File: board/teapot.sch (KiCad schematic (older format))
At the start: 42 parts, among them P1 BATT, P2 SMA, Q1 TEPT4400, U1 TLV61225, U2 microusb-b, U3 RFM69W, U4 STM32L052K8, U5 HTU21D, U6 MS5637, U7 SWD, U8 TPS79333DBVR, Y1 32.768k

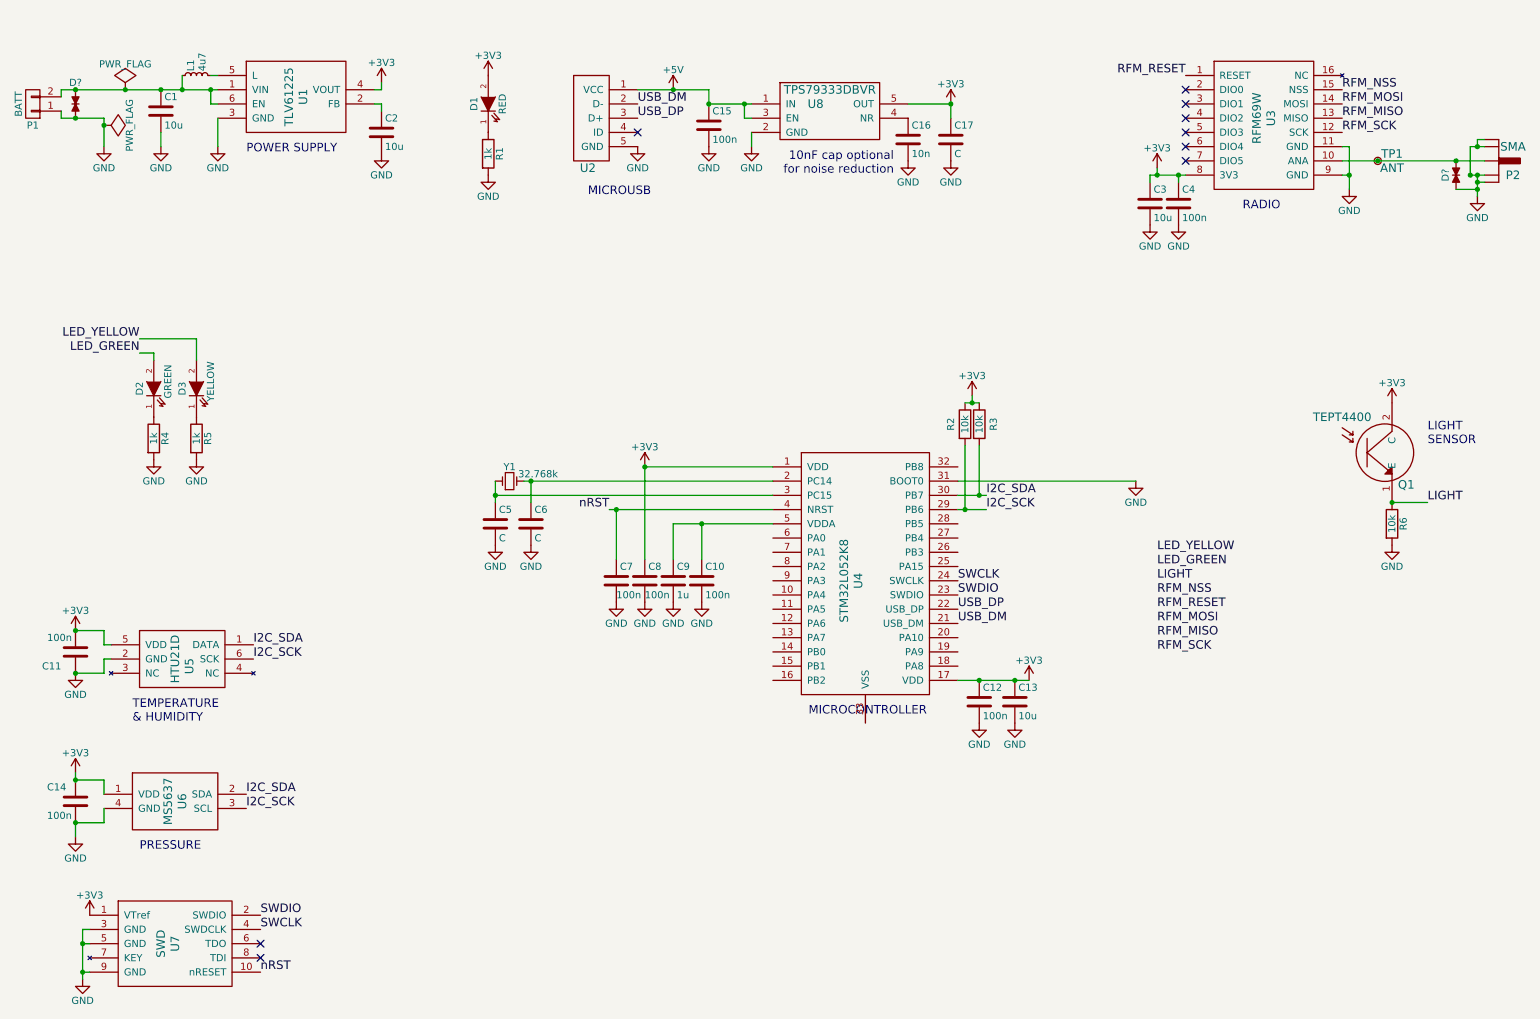
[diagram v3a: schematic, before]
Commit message: Finished speccings parts and footprints.
Resolves #3
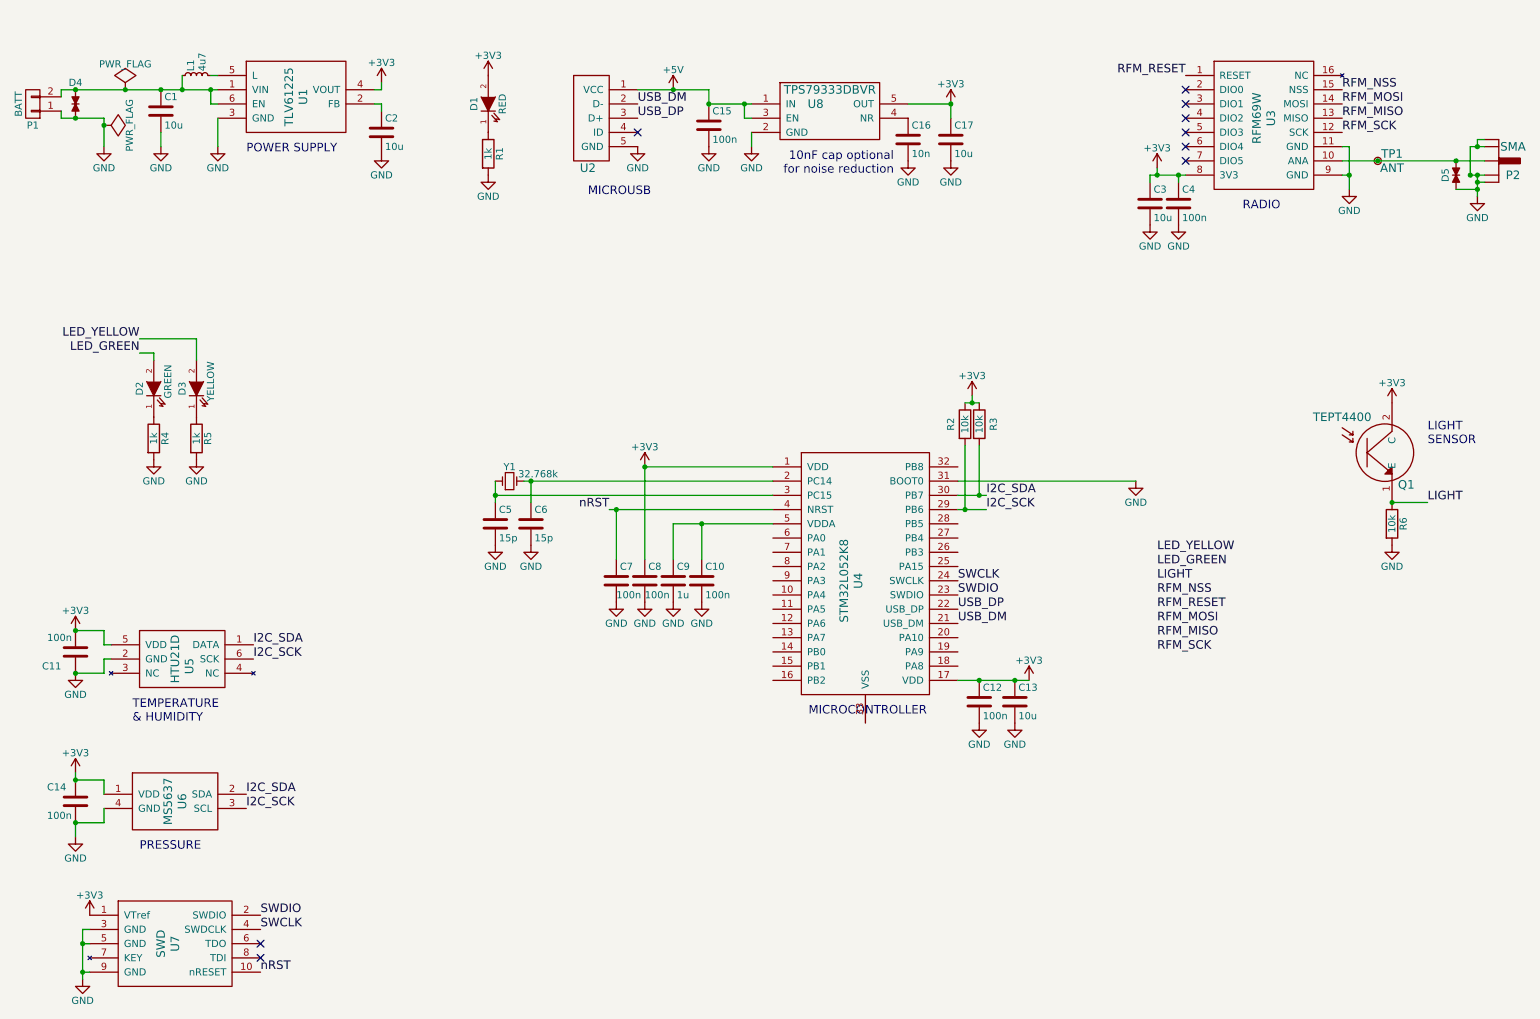
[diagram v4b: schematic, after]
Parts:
- C1, C2: footprint (none) -> Capacitors_SMD:C_0603
- C10, C11, C12, C14, C15, C4, C7, C8: footprint (none) -> Capacitors_SMD:C_0805; Farnell (none) -> 2407344
- C13, C3: footprint (none) -> Capacitors_SMD:C_0603; Farnell (none) -> 1735528
- C17: value C -> 10u; footprint (none) -> Capacitors_SMD:C_0603; Farnell (none) -> 1735528
- C5, C6: value C -> 15p; footprint (none) -> Capacitors_SMD:C_0805; Farnell (none) -> 1759193
- C9: footprint (none) -> Capacitors_SMD:C_0805; Farnell (none) -> 2496995
- D1: footprint (none) -> LEDs:LED-0805; Farnell (none) -> 2099241
- D2: footprint (none) -> LEDs:LED-0805; Farnell (none) -> 2290331
- D3: footprint (none) -> LEDs:LED-0805; Farnell (none) -> 2099242
- L1: footprint (none) -> footprints:Inductor_1212
- R1, R4, R5: footprint (none) -> Resistors_SMD:R_0805; Farnell (none) -> 2331796
- R2, R3, R6: footprint (none) -> Resistors_SMD:R_0805; Farnell (none) -> 2502786
- U2: Farnell (none) -> 2443111
- Y1: footprint (none) -> footprints:XTAL_1206
- gave numbers to parts that had none: 2
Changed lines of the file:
@@
 F 0 "C11" H 1050 5150 50  0000 L CNN
 F 1 "100n" H 975 4950 50  0000 L CNN
-F 2 "" H 988 4900 50  0000 C CNN
+F 2 "Capacitors_SMD:C_0805" H 988 4900 50  0001 C CNN
 F 3 "" H 950 5050 50  0000 C CNN
+F 4 "2407344" H 950 5050 60  0001 C CNN "Farnell"
 	1    950  5050
 	-1   0    0    1
@@
 F 0 "C2" H 3125 1500 50  0000 L CNN
 F 1 "10u" H 3125 1300 50  0000 L CNN
-F 2 "" H 3138 1250 50  0000 C CNN
-F 3 "" H 3100 1400 50  0000 C CNN
+F 2 "Capacitors_SMD:C_0603" H 3138 1250 50  0001 C CNN
+F 3 "http://www.farnell.com/datasheets/1747457.pdf" H 3100 1400 50  0001 C CNN
 F 4 "1735528" H 3100 1400 60  0001 C CNN "Farnell"
 	1    3100 1400
@@
 F 0 "C1" H 1575 1350 50  0000 L CNN
 F 1 "10u" H 1575 1150 50  0000 L CNN
-F 2 "" H 1588 1100 50  0000 C CNN
-F 3 "" H 1550 1250 50  0000 C CNN
+F 2 "Capacitors_SMD:C_0603" H 1588 1100 50  0001 C CNN
+F 3 "http://www.farnell.com/datasheets/1747457.pdf" H 1550 1250 50  0001 C CNN
 F 4 "1735528" H 1550 1250 60  0001 C CNN "Farnell"
 	1    1550 1250
@@
 F 0 "L1" H 1830 1040 50  0000 L CNN
 F 1 "4u7" H 1830 960 50  0000 L CNN
-F 2 "" H 1800 1000 50  0000 C CNN
-F 3 "" H 1800 1000 50  0000 C CNN
+F 2 "footprints:Inductor_1212" H 1800 1000 50  0001 C CNN
+F 3 "http://www.farnell.com/datasheets/1888724.pdf" H 1800 1000 50  0001 C CNN
 F 4 "2470318" H 1800 1000 60  0001 C CNN "Farnell"
 	1    1800 1000
@@
 F 0 "R3" V 7400 3450 50  0000 C CNN
 F 1 "10k" V 7300 3450 50  0000 C CNN
-F 2 "" V 7230 3450 50  0000 C CNN
+F 2 "Resistors_SMD:R_0805" V 7230 3450 50  0001 C CNN
 F 3 "" H 7300 3450 50  0000 C CNN
+F 4 "2502786" H 7300 3450 60  0001 C CNN "Farnell"
 	1    7300 3450
 	1    0    0    -1
@@
 F 0 "R2" V 7100 3450 50  0000 C CNN
 F 1 "10k" V 7200 3450 50  0000 C CNN
-F 2 "" V 7130 3450 50  0000 C CNN
+F 2 "Resistors_SMD:R_0805" V 7130 3450 50  0001 C CNN
 F 3 "" H 7200 3450 50  0000 C CNN
+F 4 "2502786" H 7200 3450 60  0001 C CNN "Farnell"
 	1    7200 3450
 	1    0    0    -1
@@
 F 0 "C14" H 750 6200 50  0000 L CNN
 F 1 "100n" H 750 6000 50  0000 L CNN
-F 2 "" H 988 5950 50  0000 C CNN
+F 2 "Capacitors_SMD:C_0805" H 988 5950 50  0001 C CNN
 F 3 "" H 950 6100 50  0000 C CNN
+F 4 "2407344" H 950 6100 60  0001 C CNN "Farnell"
 	1    950  6100
 	1    0    0    -1
@@
 F 0 "R6" V 10280 4150 50  0000 C CNN
 F 1 "10k" V 10200 4150 50  0000 C CNN
-F 2 "" V 10130 4150 50  0000 C CNN
+F 2 "Resistors_SMD:R_0805" V 10130 4150 50  0001 C CNN
 F 3 "" H 10200 4150 50  0000 C CNN
+F 4 "2502786" H 10200 4150 60  0001 C CNN "Farnell"
 	1    10200 4150
 	1    0    0    -1
@@
 F 1 "RFM69W" V 9250 1300 60  0000 C CNN
 F 2 "footprints:RFM69" H 9350 1750 60  0001 C CNN
-F 3 "https://hasnet.supplies/static/RFM69W-V1.3.pdf" H 9350 1750 60  0001 C CNN
+F 3 "http://www.hoperf.com/upload/rf/RFM69W-V1.3.pdf" H 9350 1750 60  0001 C CNN
 	1    9300 1300
 	1    0    0    -1
@@
 F 0 "C4" H 8725 2000 50  0000 L CNN
 F 1 "100n" H 8725 1800 50  0000 L CNN
-F 2 "" H 8738 1750 50  0000 C CNN
+F 2 "Capacitors_SMD:C_0805" H 8738 1750 50  0001 C CNN
 F 3 "" H 8700 1900 50  0000 C CNN
+F 4 "2407344" H 8700 1900 60  0001 C CNN "Farnell"
 	1    8700 1900
 	1    0    0    -1
@@
 F 0 "C3" H 8525 2000 50  0000 L CNN
 F 1 "10u" H 8525 1800 50  0000 L CNN
-F 2 "" H 8538 1750 50  0000 C CNN
-F 3 "" H 8500 1900 50  0000 C CNN
+F 2 "Capacitors_SMD:C_0603" H 8538 1750 50  0001 C CNN
+F 3 "http://www.farnell.com/datasheets/1747457.pdf" H 8500 1900 50  0001 C CNN
+F 4 "1735528" H 8500 1900 60  0001 C CNN "Farnell"
 	1    8500 1900
 	1    0    0    -1
@@
 F 0 "D1" H 3850 1300 50  0000 C CNN
 F 1 "RED" H 3850 1100 50  0000 C CNN
-F 2 "" H 3850 1200 50  0000 C CNN
+F 2 "LEDs:LED-0805" H 3850 1200 50  0001 C CNN
 F 3 "" H 3850 1200 50  0000 C CNN
+F 4 "2099241" H 3850 1200 60  0001 C CNN "Farnell"
 	1    3850 1200
 	0    -1   -1   0
@@
 F 0 "R1" V 3930 1550 50  0000 C CNN
 F 1 "1k" V 3850 1550 50  0000 C CNN
-F 2 "" V 3780 1550 50  0000 C CNN
+F 2 "Resistors_SMD:R_0805" V 3780 1550 50  0001 C CNN
 F 3 "" H 3850 1550 50  0000 C CNN
+F 4 "2331796" H 3850 1550 60  0001 C CNN "Farnell"
 	1    3850 1550
 	1    0    0    -1
@@
 F 0 "D2" H 1500 3300 50  0000 C CNN
 F 1 "GREEN" H 1550 3100 50  0000 C CNN
-F 2 "" H 1500 3200 50  0000 C CNN
+F 2 "LEDs:LED-0805" H 1500 3200 50  0001 C CNN
 F 3 "" H 1500 3200 50  0000 C CNN
+F 4 "2290331" H 1500 3200 60  0001 C CNN "Farnell"
 	1    1500 3200
 	0    -1   -1   0
@@
 F 0 "D3" H 1800 3300 50  0000 C CNN
 F 1 "YELLOW" H 1850 3100 50  0000 C CNN
-F 2 "" H 1800 3200 50  0000 C CNN
+F 2 "LEDs:LED-0805" H 1800 3200 50  0001 C CNN
 F 3 "" H 1800 3200 50  0000 C CNN
+F 4 "2099242" H 1800 3200 60  0001 C CNN "Farnell"
 	1    1800 3200
 	0    -1   -1   0
@@
 F 0 "R4" V 1580 3550 50  0000 C CNN
 F 1 "1k" V 1500 3550 50  0000 C CNN
-F 2 "" V 1430 3550 50  0000 C CNN
+F 2 "Resistors_SMD:R_0805" V 1430 3550 50  0001 C CNN
 F 3 "" H 1500 3550 50  0000 C CNN
+F 4 "2331796" H 1500 3550 60  0001 C CNN "Farnell"
 	1    1500 3550
 	1    0    0    -1
@@
 F 0 "R5" V 1880 3550 50  0000 C CNN
 F 1 "1k" V 1800 3550 50  0000 C CNN
-F 2 "" V 1730 3550 50  0000 C CNN
+F 2 "Resistors_SMD:R_0805" V 1730 3550 50  0001 C CNN
 F 3 "" H 1800 3550 50  0000 C CNN
+F 4 "2331796" H 1800 3550 60  0001 C CNN "Farnell"
 	1    1800 3550
 	1    0    0    -1
@@
 F 0 "C7" H 4775 4650 50  0000 L CNN
 F 1 "100n" H 4750 4450 50  0000 L CNN
-F 2 "" H 4788 4400 50  0000 C CNN
+F 2 "Capacitors_SMD:C_0805" H 4788 4400 50  0001 C CNN
 F 3 "" H 4750 4550 50  0000 C CNN
+F 4 "2407344" H 4750 4550 60  0001 C CNN "Farnell"
 	1    4750 4550
 	1    0    0    -1
@@
 F 0 "C8" H 4975 4650 50  0000 L CNN
 F 1 "100n" H 4950 4450 50  0000 L CNN
-F 2 "" H 4988 4400 50  0000 C CNN
+F 2 "Capacitors_SMD:C_0805" H 4988 4400 50  0001 C CNN
 F 3 "" H 4950 4550 50  0000 C CNN
+F 4 "2407344" H 4950 4550 60  0001 C CNN "Farnell"
 	1    4950 4550
 	1    0    0    -1
@@
 F 0 "C12" H 7325 5500 50  0000 L CNN
 F 1 "100n" H 7325 5300 50  0000 L CNN
-F 2 "" H 7338 5250 50  0000 C CNN
+F 2 "Capacitors_SMD:C_0805" H 7338 5250 50  0001 C CNN
 F 3 "" H 7300 5400 50  0000 C CNN
+F 4 "2407344" H 7300 5400 60  0001 C CNN "Farnell"
 	1    7300 5400
 	1    0    0    -1
@@
 F 0 "C13" H 7575 5500 50  0000 L CNN
 F 1 "10u" H 7575 5300 50  0000 L CNN
-F 2 "" H 7588 5250 50  0000 C CNN
-F 3 "" H 7550 5400 50  0000 C CNN
+F 2 "Capacitors_SMD:C_0603" H 7588 5250 50  0001 C CNN
+F 3 "http://www.farnell.com/datasheets/1747457.pdf" H 7550 5400 50  0001 C CNN
+F 4 "1735528" H 7550 5400 60  0001 C CNN "Farnell"
 	1    7550 5400
 	1    0    0    -1
@@
 F 0 "C9" H 5175 4650 50  0000 L CNN
 F 1 "1u" H 5175 4450 50  0000 L CNN
-F 2 "" H 5188 4400 50  0000 C CNN
+F 2 "Capacitors_SMD:C_0805" H 5188 4400 50  0001 C CNN
 F 3 "" H 5150 4550 50  0000 C CNN
+F 4 "2496995" H 5150 4550 60  0001 C CNN "Farnell"
 	1    5150 4550
 	1    0    0    -1
@@
 F 0 "C10" H 5375 4650 50  0000 L CNN
 F 1 "100n" H 5375 4450 50  0000 L CNN
-F 2 "" H 5388 4400 50  0000 C CNN
+F 2 "Capacitors_SMD:C_0805" H 5388 4400 50  0001 C CNN
 F 3 "" H 5350 4550 50  0000 C CNN
+F 4 "2407344" H 5350 4550 60  0001 C CNN "Farnell"
 	1    5350 4550
 	1    0    0    -1
@@
 F 0 "Y1" H 4000 3950 50  0000 C CNN
 F 1 "32.768k" H 4200 3900 50  0000 C CNN
-F 2 "" H 4000 3850 50  0000 C CNN
+F 2 "footprints:XTAL_1206" H 4000 3850 50  0001 C CNN
 F 3 "http://www.farnell.com/datasheets/1883680.pdf" H 4000 3850 50  0001 C CNN
 F 4 "2101347" H 4000 3850 60  0001 C CNN "Farnell"
@@
 P 3900 4150
 F 0 "C5" H 3925 4250 50  0000 L CNN
-F 1 "C" H 3925 4050 50  0000 L CNN
-F 2 "" H 3938 4000 50  0000 C CNN
+F 1 "15p" H 3925 4050 50  0000 L CNN
+F 2 "Capacitors_SMD:C_0805" H 3938 4000 50  0001 C CNN
 F 3 "" H 3900 4150 50  0000 C CNN
+F 4 "1759193" H 3900 4150 60  0001 C CNN "Farnell"
 	1    3900 4150
 	1    0    0    -1
@@
 P 4150 4150
 F 0 "C6" H 4175 4250 50  0000 L CNN
-F 1 "C" H 4175 4050 50  0000 L CNN
-F 2 "" H 4188 4000 50  0000 C CNN
+F 1 "15p" H 4175 4050 50  0000 L CNN
+F 2 "Capacitors_SMD:C_0805" H 4188 4000 50  0001 C CNN
 F 3 "" H 4150 4150 50  0000 C CNN
+F 4 "1759193" H 4150 4150 60  0001 C CNN "Farnell"
 	1    4150 4150
 	1    0    0    -1
@@
 F 2 "footprints:USB3065" H 4700 1300 60  0001 C CNN
 F 3 "" H 4700 1300 60  0000 C CNN
+F 4 "2443111" H 4600 1300 60  0001 C CNN "Farnell"
 	1    4600 1300
 	1    0    0    -1
@@
 F 0 "C15" H 5425 1450 50  0000 L CNN
 F 1 "100n" H 5425 1250 50  0000 L CNN
-F 2 "" H 5438 1200 50  0000 C CNN
+F 2 "Capacitors_SMD:C_0805" H 5438 1200 50  0001 C CNN
 F 3 "" H 5400 1350 50  0000 C CNN
+F 4 "2407344" H 5400 1350 60  0001 C CNN "Farnell"
 	1    5400 1350
 	1    0    0    -1
@@
 P 7100 1450
 F 0 "C17" H 7125 1550 50  0000 L CNN
-F 1 "C" H 7125 1350 50  0000 L CNN
-F 2 "" H 7138 1300 50  0000 C CNN
-F 3 "" H 7100 1450 50  0000 C CNN
+F 1 "10u" H 7125 1350 50  0000 L CNN
+F 2 "Capacitors_SMD:C_0603" H 7138 1300 50  0001 C CNN
+F 3 "http://www.farnell.com/datasheets/1747457.pdf" H 7100 1450 50  0001 C CNN
+F 4 "1735528" H 7100 1450 60  0001 C CNN "Farnell"
 	1    7100 1450
 	1    0    0    -1
@@
 Connection ~ 10650 1600
 $Comp
-L TVS_small D?
+L TVS_small D4
 U 1 1 56786E75
 P 950 1200
-F 0 "D?" V 800 1200 50  0000 C CNN
+F 0 "D4" V 800 1200 50  0000 C CNN
 F 1 "TVS_small" H 950 1125 50  0001 C CNN
 F 2 "Resistors_SMD:R_0603" H 950 1200 60  0001 C CNN
@@
 	1150 1300 1150 1500
 $Comp
-L TVS_small D?
+L TVS_small D5
 U 1 1 56787864
 P 10650 1700
-F 0 "D?" H 10650 1775 50  0000 C CNN
+F 0 "D5" H 10650 1775 50  0000 C CNN
 F 1 "TVS_small" H 10650 1625 50  0001 C CNN
 F 2 "Resistors_SMD:R_0603" H 10650 1700 60  0001 C CNN

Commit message: Fixed a couple of footprint derps
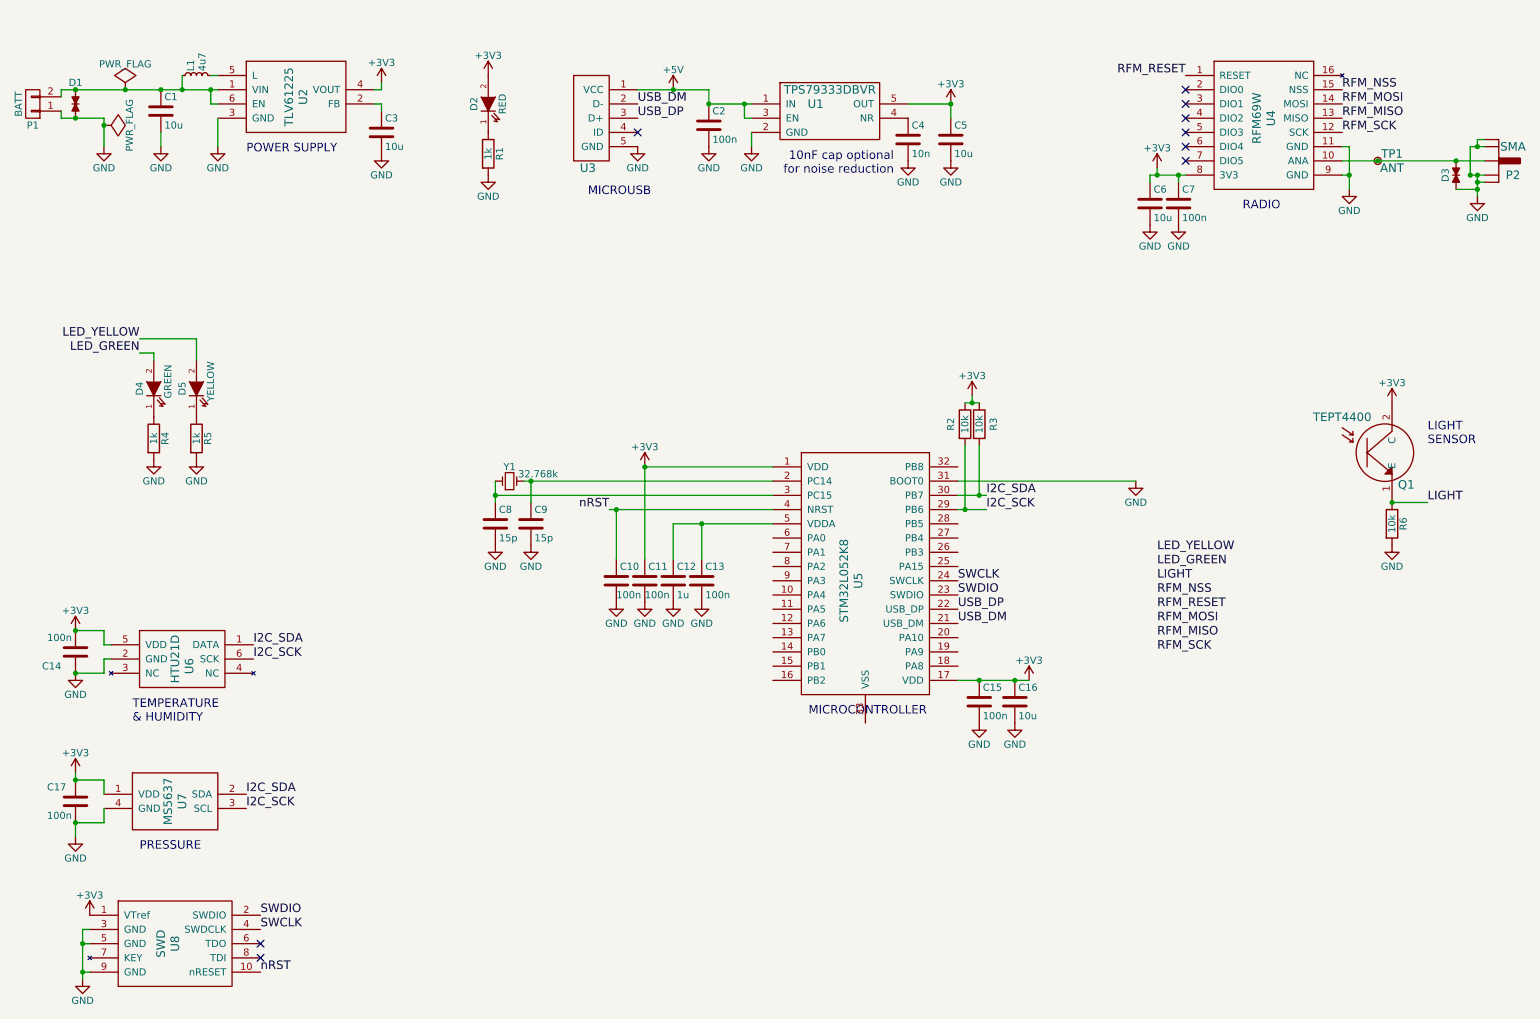
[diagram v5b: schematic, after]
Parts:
- U2: renamed from U1; footprint footprints:SC-70 -> (none)
- renumbered C7 to C10, C8 to C11, C9 to C12, C10 to C13, C11 to C14, C12 to C15, C13 to C16, C14 to C17, C15 to C2, C2 to C3, C16 to C4, C17 to C5, C3 to C6, C4 to C7, C5 to C8, C6 to C9, D4 to D1, D1 to D2, D5 to D3, D2 to D4, D3 to D5, U8 to U1, U2 to U3, U3 to U4, U4 to U5, U5 to U6, U6 to U7, U7 to U8
